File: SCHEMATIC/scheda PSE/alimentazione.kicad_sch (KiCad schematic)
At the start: 40 parts, among them J2 Vin, J3 USB_B_Mini, J4 Vout 5V, SW7 Power_button, U5 TPS563201, U6 XC6705A331MR-G

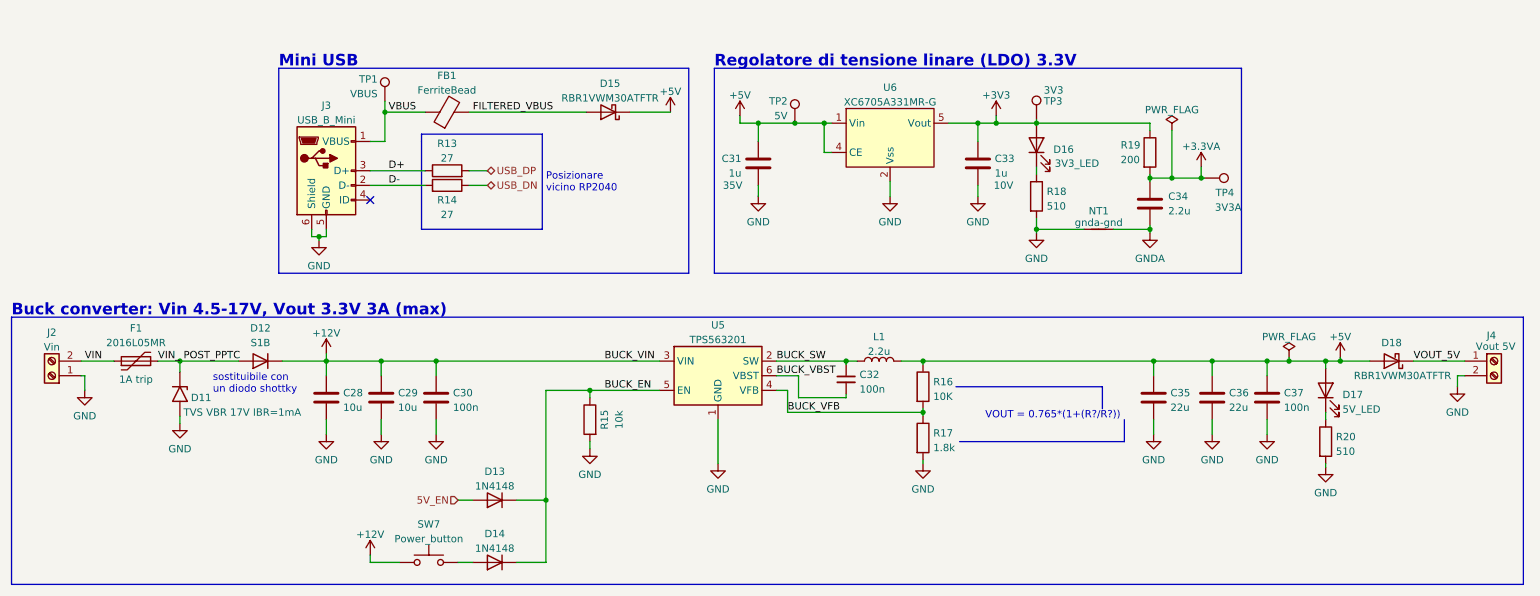
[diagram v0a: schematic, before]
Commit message: Aggiunte tutte le cose richieste dal prof
Aggiunte tutte le cose richieste dal prof:
wifi
servo
uscita led
MANCA DA METERE IL SOLDER MASK SUI PAD NON USATI DEL GPS
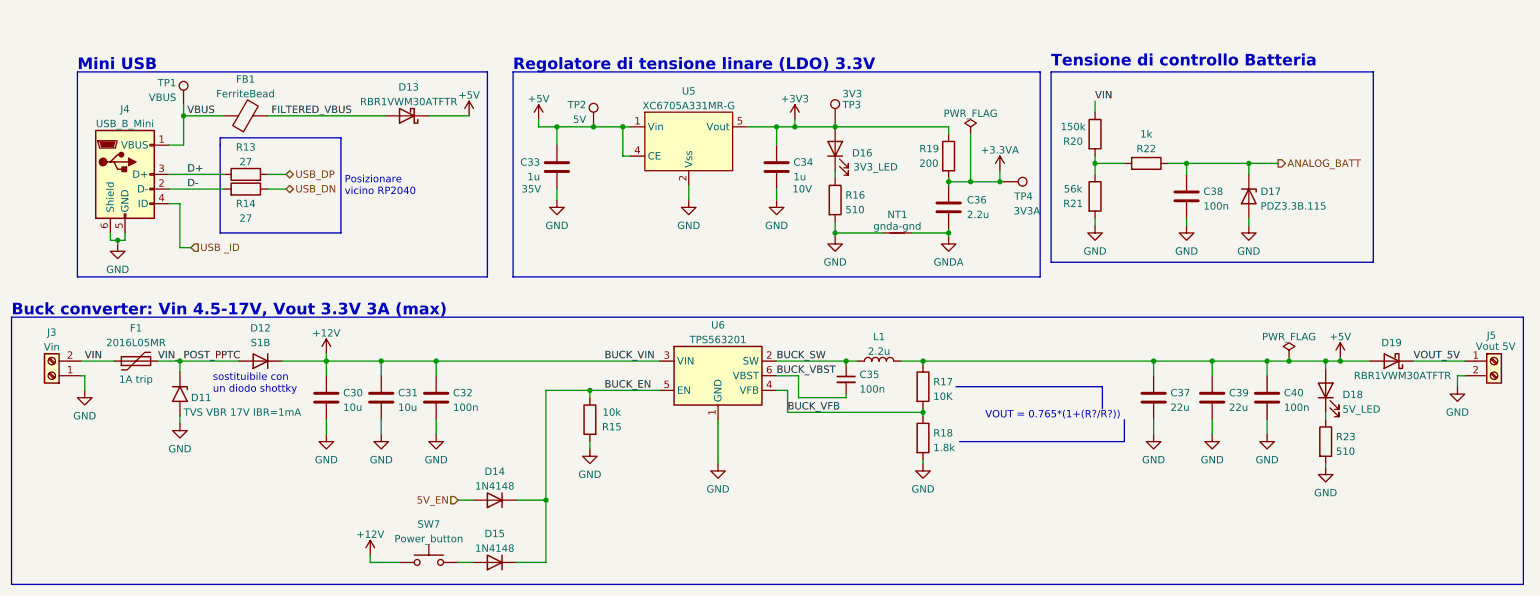
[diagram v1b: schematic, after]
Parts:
- added C38: 100n, Capacitor_SMD:C_0603_1608Metric, symbol Device:C
- added D17: PDZ3.3B.115, Diode_SMD:D_SOD-323_HandSoldering, symbol Device:D_Zener
- added R20: 150k, Resistor_SMD:R_0603_1608Metric, symbol Device:R
- added R21: 56k, Resistor_SMD:R_0603_1608Metric, symbol Device:R
- added R22: 1k, Resistor_SMD:R_0603_1608Metric, symbol Device:R
- renumbered C28 to C30, C29 to C31, C30 to C32, C31 to C33, C33 to C34, C32 to C35, C34 to C36, C35 to C37, C36 to C39, C37 to C40, D15 to D13, D13 to D14, D14 to D15, D17 to D18, D18 to D19, J2 to J3, J3 to J4, J4 to J5, R18 to R16, R16 to R17, R17 to R18, R20 to R23, U6 to U5, U5 to U6
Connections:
- net GND: now also C38.2, D17.2 (A), R21.2
- net VIN: now also R20.1
- net USB _ID: now reaches J4.4 (ID)
- new net: R20.2, R21.1, R22.2
- new net ANALOG_BATT: C38.1, D17.1 (K), R22.1
- no-connect marks 1 -> 0
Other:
- note added: "Tensione di controllo Batteria"
- moved on the sheet: C33, C34, C36, D13, D16, FB1, J4, NT1, R13, R14, R16, R19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

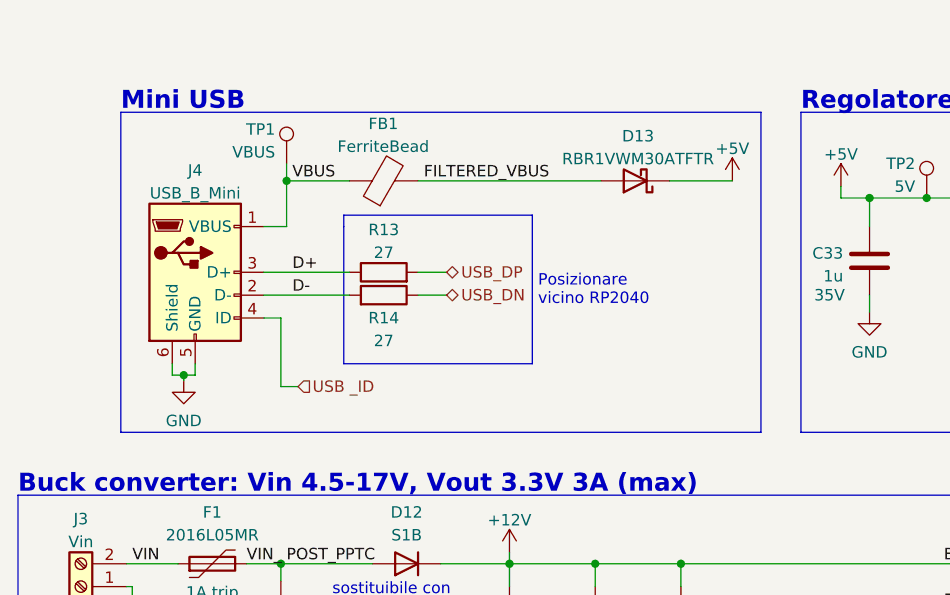
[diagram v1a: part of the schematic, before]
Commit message: Aggiunto mosfet uscita corrente usb
Ultima modifica prima della revisone generale.
aggiunto un mosfet P per l'attivazione dell'uscita della tensione alla usb in caso di master
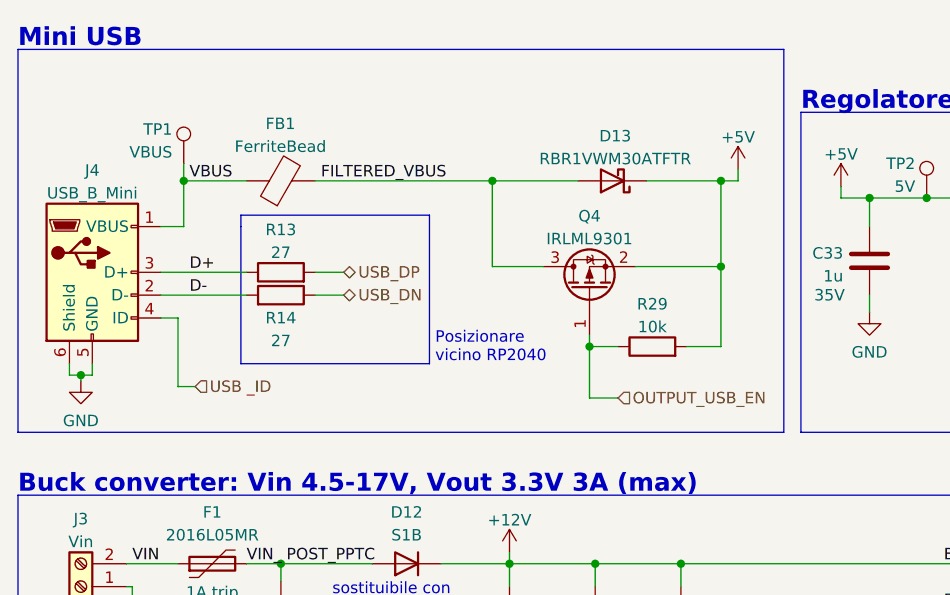
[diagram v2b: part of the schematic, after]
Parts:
- added Q4: IRLML9301, Package_TO_SOT_SMD:SOT-23, symbol Transistor_FET:IRLML9301
- added R29: 10k, Resistor_SMD:R_0603_1608Metric, symbol Device:R
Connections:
- net +5V: now also Q4.2 (S), R29.2
- net FILTERED_VBUS: now also Q4.3 (D)
- new net OUTPUT_USB_EN: Q4.1 (G), R29.1
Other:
- moved on the sheet: D13, FB1, J4, R13, R14, TP1

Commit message: Versione definitiva inviata ai prof
Sistemato tutto e inviato il tutto ai prof
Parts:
- added R30: 47k, Resistor_SMD:R_0603_1608Metric, symbol Device:R
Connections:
- net GND: now also R30.2
- net USB _ID: now also R30.1
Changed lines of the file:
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@@
   (junction (at 97.155 62.865) (diameter 0) (color 0 0 0 0)
   )
+  (junction (at 36.195 68.58) (diameter 0) (color 0 0 0 0)
+  )
   (junction (at 119.38 100.965) (diameter 0) (color 0 0 0 0)
   )
@@
     (stroke (width 0) (type default) (color 0 0 0 0))
   )
-  (wire (pts (xy 36.83 68.58) (xy 36.83 76.2))
-    (stroke (width 0) (type default) (color 0 0 0 0))
-  )
   (polyline (pts (xy 255.27 45.72) (xy 199.39 45.72))
     (stroke (width 0) (type default) (color 0 0 0 0))
@@
     (stroke (width 0) (type default) (color 0 0 0 0))
   )
+  (wire (pts (xy 41.91 76.835) (xy 43.815 76.835))
+    (stroke (width 0) (type default) (color 0 0 0 0))
+  )
   (wire (pts (xy 125.095 60.325) (xy 125.095 55.245))
     (stroke (width 0) (type default) (color 0 0 0 0))
@@
     (stroke (width 0) (type default) (color 0 0 0 0))
   )
+  (wire (pts (xy 34.925 68.58) (xy 36.195 68.58))
+    (stroke (width 0) (type default) (color 0 0 0 0))
+  )
   (wire (pts (xy 222.885 61.595) (xy 233.68 61.595))
     (stroke (width 0) (type default) (color 0 0 0 0))
@@
     (stroke (width 0) (type default) (color 0 0 0 0))
   )
+  (wire (pts (xy 36.195 76.835) (xy 36.195 77.47))
+    (stroke (width 0) (type default) (color 0 0 0 0))
+  )
   (wire (pts (xy 151.765 98.425) (xy 155.575 98.425))
     (stroke (width 0) (type default) (color 0 0 0 0))
@@
     (stroke (width 0) (type default) (color 0 0 0 0))
   )
-  (wire (pts (xy 36.83 76.2) (xy 38.735 76.2))
-    (stroke (width 0) (type default) (color 0 0 0 0))
-  )
   (wire (pts (xy 173.355 95.885) (xy 177.165 95.885))
     (stroke (width 0) (type default) (color 0 0 0 0))
@@
     (stroke (width 0) (type default) (color 0 0 0 0))
   )
+  (wire (pts (xy 36.195 68.58) (xy 41.91 68.58))
+    (stroke (width 0) (type default) (color 0 0 0 0))
+  )
+  (wire (pts (xy 36.195 68.58) (xy 36.195 69.215))
+    (stroke (width 0) (type default) (color 0 0 0 0))
+  )
   (wire (pts (xy 113.665 66.04) (xy 113.665 67.945))
     (stroke (width 0) (type default) (color 0 0 0 0))
@@
     (stroke (width 0) (type default) (color 0 0 0 0))
   )
-  (wire (pts (xy 34.925 68.58) (xy 36.83 68.58))
-    (stroke (width 0) (type default) (color 0 0 0 0))
-  )
   (wire (pts (xy 119.38 100.965) (xy 119.38 102.235))
     (stroke (width 0) (type default) (color 0 0 0 0))
@@
   )
   (wire (pts (xy 207.01 61.595) (xy 207.01 63.5))
+    (stroke (width 0) (type default) (color 0 0 0 0))
+  )
+  (wire (pts (xy 41.91 68.58) (xy 41.91 76.835))
     (stroke (width 0) (type default) (color 0 0 0 0))
   )
@@
     (effects (font (size 1.27 1.27)) (justify left))
   )
-  (hierarchical_label "USB _ID" (shape input) (at 38.735 76.2 0)
+  (hierarchical_label "USB _ID" (shape input) (at 43.815 76.835 0)
     (effects (font (size 1.27 1.27)) (justify left))
   )
@@
     (pin "2")
   )
+  (symbol (lib_id "power:GND") (at 36.195 77.47 0) (unit 1)
+    (in_bom yes) (on_board yes) (fields_autoplaced)
+    (property "Reference" "#PWR0106" (id 0) (at 36.195 83.82 0)
+      (effects (font (size 1.27 1.27)) hide)
+    )
+    (property "Value" "GND" (id 1) (at 36.195 81.9134 0))
+    (property "Footprint" "" (id 2) (at 36.195 77.47 0)
+      (effects (font (size 1.27 1.27)) hide)
+    )
+    (property "Datasheet" "" (id 3) (at 36.195 77.47 0)
+      (effects (font (size 1.27 1.27)) hide)
+    )
+    (pin "1")
+  )
   (symbol (lib_id "power:+3.3VA") (at 190.5 62.865 0) (unit 1)
     (in_bom yes) (on_board yes) (fields_autoplaced)
@@
       (effects (font (size 1.27 1.27)) hide)
     )
+    (pin "1")
+    (pin "2")
+  )
+  (symbol (lib_id "Device:R") (at 36.195 73.025 0) (mirror y) (unit 1)
+    (in_bom yes) (on_board yes)
+    (property "Reference" "R30" (id 0) (at 39.37 72.39 0))
+    (property "Value" "47k" (id 1) (at 39.37 74.93 0))
+    (property "Footprint" "Resistor_SMD:R_0603_1608Metric" (id 2) (at 37.973 73.025 90)
+      (effects (font (size 1.27 1.27)) hide)
+    )
+    (property "Datasheet" "~" (id 3) (at 36.195 73.025 0)
+      (effects (font (size 1.27 1.27)) hide)
+    )
